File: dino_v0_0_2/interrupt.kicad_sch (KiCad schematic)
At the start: 16 parts, among them U18 74LS373, U22 74LS02, U25 74LS245, U34 74LS373, U37 74LS04, U39 74LS00, U72 74LS245, U73 74LS245

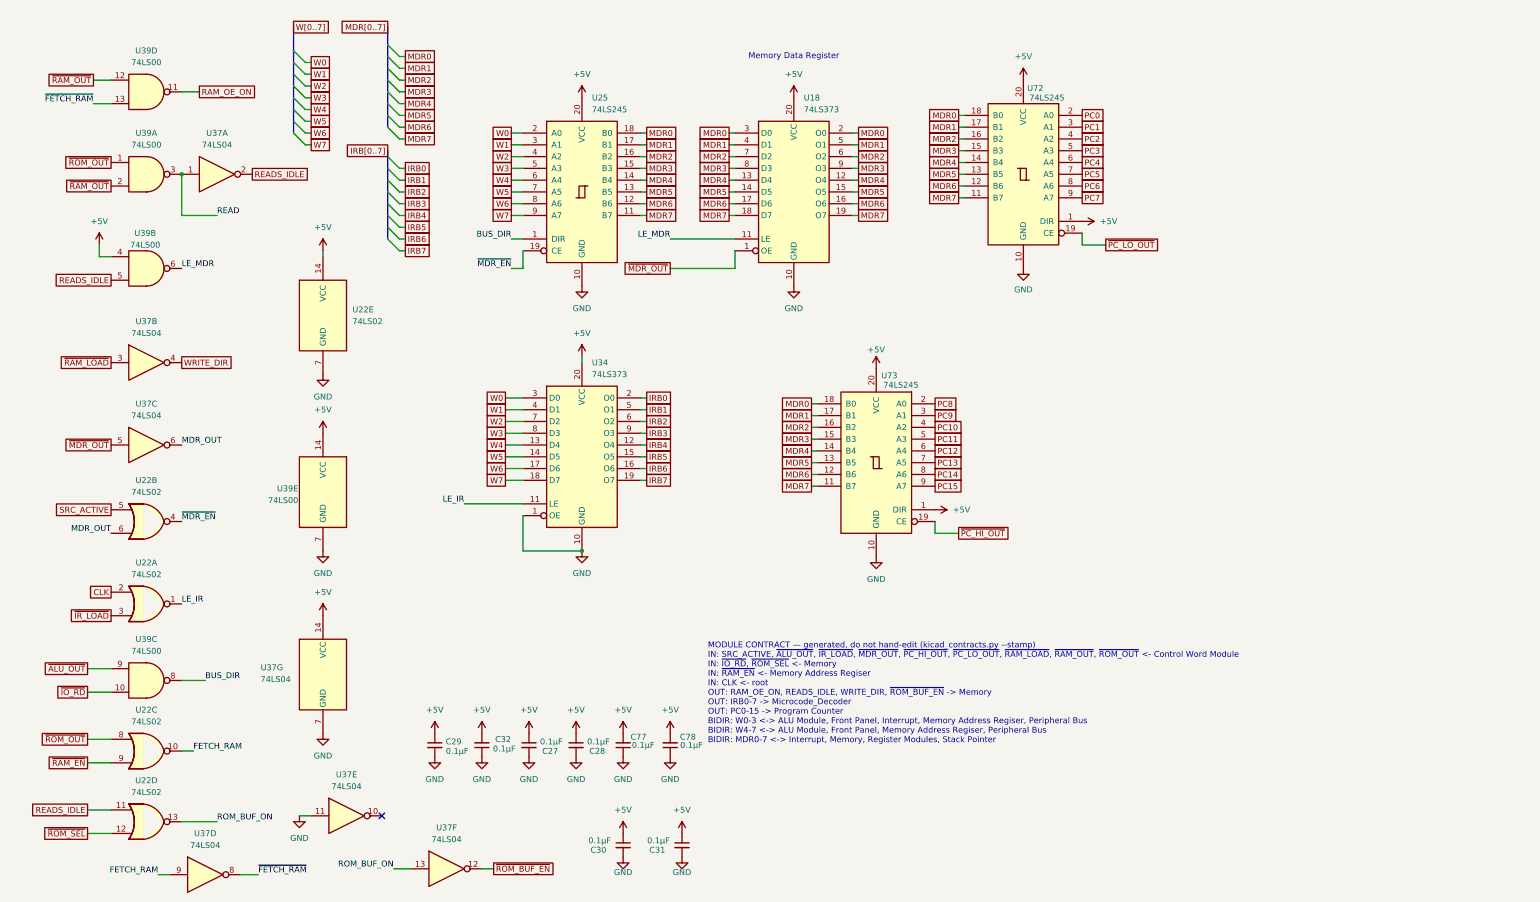
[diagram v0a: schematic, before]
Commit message: feat(int): draw the interrupt block; sheet cleanup pass
New sheet dino_v0_0_2/interrupt.kicad_sch (page 15): U80-U87, R28 4.7k
pull-up on ~{IRQ}, R29 100R on the block's CLK branch, C83-C90. Every
pin per PHASE_INT SECTION 3, checked against the plan with kicad_netlist
and kicad-cli (146 pins, 0 mismatches).

Old sheets (SECTION 3.2): U28.4 lifted off GND to INJECT; U61.3 to
END_OR_ACCEPT; U36.1 to PC_UP_GATED; U49 D0-3 cut from U48 Za-Zd and
routed through U87 as FLAG_NEXT0-3 / FLAG_D0-3; FLAG_C/Z/V/N and the
five decoder outputs made global. dino_serial: U104 74LS05, INTR ->
~{IRQ}, C4.

Placement pass on every sheet: bus entries and global labels no longer
share wires; M, CW, T, IRB and SA buses kept as labelled keys. Nets
diffed against HEAD per sheet: only the intended changes and a rotated
C29. Project ERC: 0 errors. MODULE CONTRACT stamps regenerated.

Co-Authored-By: Claude Fable 5.1 <noreply@anthropic.com>
Claude-Session: https://claude.ai/code/session_01JGxSS4MVUcaZdKZGtKroSg
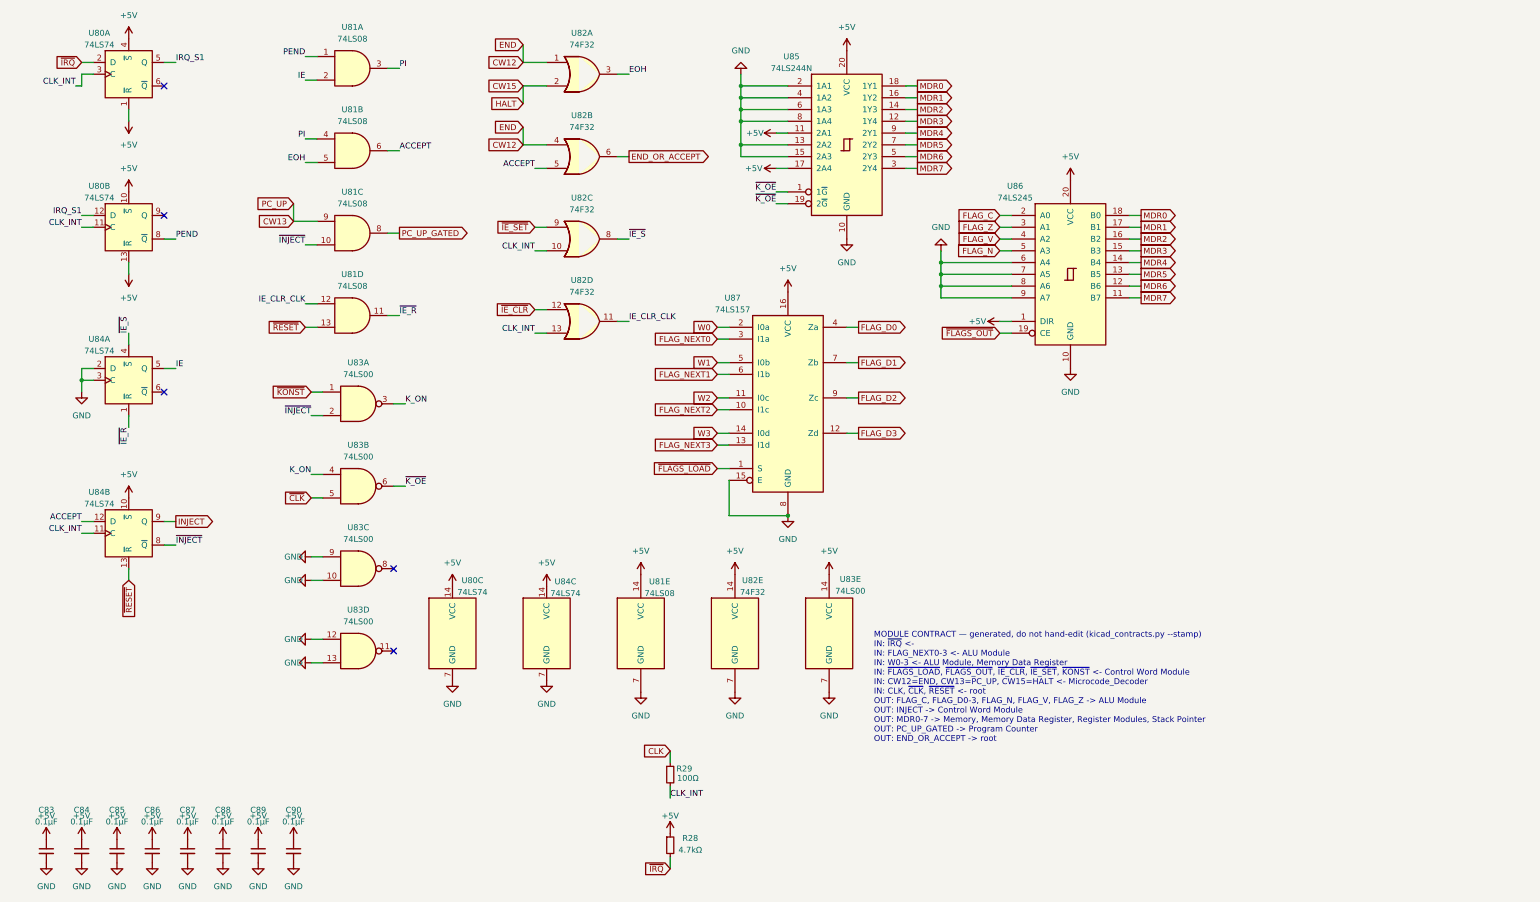
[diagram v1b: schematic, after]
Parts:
- removed C27, C28, C29, C30, C31, C32, C77, C78: 0.1µF, Capacitor_THT:C_Disc_D5.0mm_W2.5mm_P2.50mm, symbol Device:C_Small
- removed U18, U34: 74LS373, Package_DIP:DIP-20_W7.62mm, symbol 74xx:74LS373
- removed U22: 74LS02, Package_DIP:DIP-14_W7.62mm, symbol 74xx:74LS02
- removed U25, U72, U73: 74LS245, Package_DIP:DIP-20_W7.62mm, symbol 74xx:74LS245
- removed U37: 74LS04, Package_DIP:DIP-14_W7.62mm, symbol 74xx:74LS04
- removed U39: 74LS00, Package_DIP:DIP-14_W7.62mm, symbol 74xx:74LS00
- added C83, C84, C85, C86, C87, C88, C89, C90: 0.1µF, Capacitor_THT:C_Disc_D5.0mm_W2.5mm_P2.50mm, symbol Device:C_Small
- added R28: 4.7kΩ, Resistor_THT:R_Axial_DIN0207_L6.3mm_D2.5mm_P10.16mm_Horizontal, symbol Device:R_Small
- added R29: 100Ω, Resistor_THT:R_Axial_DIN0207_L6.3mm_D2.5mm_P10.16mm_Horizontal, symbol Device:R_Small
- added U80, U84: 74LS74, Package_DIP:DIP-14_W7.62mm, symbol 74xx:74LS74
- added U81: 74LS08, Package_DIP:DIP-14_W7.62mm, symbol 74xx:74LS08
- added U82: 74F32, Package_DIP:DIP-14_W7.62mm, symbol 74xx:74LS32
- added U83: 74LS00, Package_DIP:DIP-14_W7.62mm, symbol 74xx:74LS00
- added U85: 74LS244N, Package_DIP:DIP-20_W7.62mm, symbol dino:74LS244N
- added U86: 74LS245, Package_DIP:DIP-20_W7.62mm, symbol 74xx:74LS245
- added U87: 74LS157, Package_DIP:DIP-16_W7.62mm, symbol 74xx:74LS157
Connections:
- net +5V: now also C83.1, C84.1, C85.1, C86.1, C87.1, C88.1, C89.1, C90.1, R28.1, U80.1 (~{R}), U80.10 (~{S}), U80.13 (~{R}), U80.14 (VCC), U80.4 (~{S}), U81.14 (VCC), U82.14 (VCC), U83.14 (VCC), U84.10 (~{S}), U84.14 (VCC), U85.11 (2A1), U85.17 (2A4), U85.20 (VCC), U86.1 (DIR), U86.20 (VCC), U87.16 (VCC)
- net CLK: now also R29.1
- net GND: now also C83.2, C84.2, C85.2, C86.2, C87.2, C88.2, C89.2, C90.2, U80.7 (GND), U81.7 (GND), U82.7 (GND), U83.10, U83.12, U83.13, U83.7 (GND), U83.9, U84.2 (D), U84.3 (C), U84.7 (GND), U85.10 (GND), U85.13 (2A2), U85.15 (2A3), U85.2 (1A1), U85.4 (1A2), U85.6 (1A3), U85.8 (1A4), U86.10 (GND), U86.6 (A4), U86.7 (A5), U86.8 (A6), U86.9 (A7), U87.15 (E), U87.8 (GND)
- net MDR0: now also U85.18 (1Y1), U86.18 (B0)
- net MDR1: now also U85.16 (1Y2), U86.17 (B1)
- net MDR2: now also U85.14 (1Y3), U86.16 (B2)
- net MDR3: now also U85.12 (1Y4), U86.15 (B3)
- net MDR4: now also U85.9 (2Y1), U86.14 (B4)
- net MDR5: now also U85.7 (2Y2), U86.13 (B5)
- net MDR6: now also U85.5 (2Y3), U86.12 (B6)
- net MDR7: now also U85.3 (2Y4), U86.11 (B7)
- net W0: now also U87.2 (I0a)
- net W1: now also U87.5 (I0b)
- net W2: now also U87.11 (I0c)
- net W3: now also U87.14 (I0d)
- new net ACCEPT: U81.6, U82.5, U84.12 (D)
- new net CLK_INT: R29.2, U80.11 (C), U80.3 (C), U82.10, U82.13, U84.11 (C)
- new net CW12: U82.1, U82.4
- new net CW13: U81.9
- new net CW15: U82.2
- new net END_OR_ACCEPT: U82.6
- new net EOH: U81.5, U82.3
- new net FLAG_C: U86.2 (A0)
- new net FLAG_D0: U87.4 (Za)
- new net FLAG_D1: U87.7 (Zb)
- new net FLAG_D2: U87.9 (Zc)
- new net FLAG_D3: U87.12 (Zd)
- new net FLAG_N: U86.5 (A3)
- new net FLAG_NEXT0: U87.3 (I1a)
- new net FLAG_NEXT1: U87.6 (I1b)
- new net FLAG_NEXT2: U87.10 (I1c)
- new net FLAG_NEXT3: U87.13 (I1d)
- new net FLAG_V: U86.4 (A2)
- new net FLAG_Z: U86.3 (A1)
- new net IE: U81.2, U84.5 (Q)
- new net IE_CLR_CLK: U81.12, U82.11
- new net INJECT: U84.9 (Q)
- new net IRQ_S1: U80.12 (D), U80.5 (Q)
- new net K_ON: U83.3, U83.4
- new net PC_UP_GATED: U81.8
- new net PEND: U80.8 (~{Q}), U81.1
- new net PI: U81.3, U81.4
- new net ~{CLK}: U83.5
- new net ~{FLAGS_LOAD}: U87.1 (S)
- new net ~{FLAGS_OUT}: U86.19 (CE)
- new net ~{IE_CLR}: U82.12
- new net ~{IE_R}: U81.11, U84.1 (~{R})
- new net ~{IE_SET}: U82.9
- new net ~{IE_S}: U82.8, U84.4 (~{S})
- new net ~{INJECT}: U81.10, U83.2, U84.8 (~{Q})
- new net ~{IRQ}: R28.2, U80.2 (D)
- new net ~{KONST}: U83.1
- new net ~{K_OE}: U83.6, U85.1 (1~{G}), U85.19 (2~{G})
- new net ~{RESET}: U81.13, U84.13 (~{R})
- no-connect marks 1 -> 5
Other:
- note added: "MODULE CONTRACT — generated, do not hand-edit (kicad_contracts.py --stamp) IN: ~{IRQ} <- IN: FLAG_NEXT0-3 <- ALU Module IN: W0-3 <- ALU Module, Memory Data Register IN: ~{FLAGS_LOAD}, ~{FLAGS_OUT}, ~{IE_CLR}, ~{IE_SET}, ~{KONST} <- Control Word Module IN: CW12=END, CW13=PC_UP, CW15=HALT <- Microcode_Decoder IN: CLK, ~{CLK}, ~{RESET} <- root OUT: FLAG_C, FLAG_D0-3, FLAG_N, FLAG_V, FLAG_Z -> ALU Mo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"
- note removed: "MODULE CONTRACT — generated, do not hand-edit (kicad_contracts.py --stamp) IN: SRC_ACTIVE, ~{ALU_OUT}, ~{IR_LOAD}, ~{MDR_OUT}, ~{PC_HI_OUT}, ~{PC_LO_OUT}, ~{RAM_LOAD}, ~{RAM_OUT}, ~{ROM_OUT} <- Control Word Module IN: ~{IO_RD}, ~{ROM_SEL} <- Memory IN: ~{RAM_EN} <- Memory Address Regiser IN: CLK <- root OUT: RAM_OE_ON, READS_IDLE, WRITE_DIR, ~{ROM_BUF_EN} -> Memory OUT: IRB0-7 -> Microcode_Decode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"
- note removed: "Memory Data Register"
